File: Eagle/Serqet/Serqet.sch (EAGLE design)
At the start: 58 parts, among them U1 AD9283, U3 LTC2633CTS8-LZ8TRMPBF

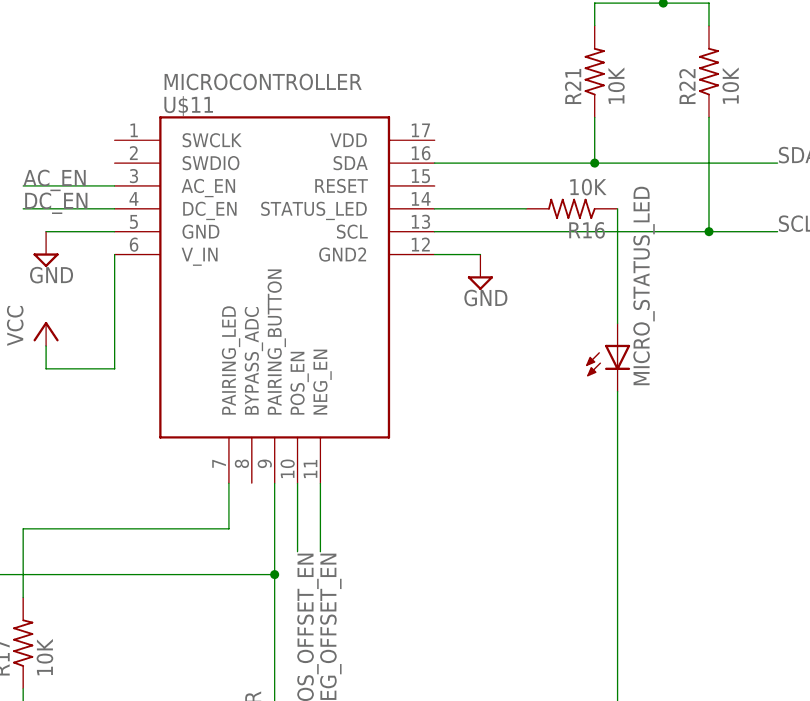
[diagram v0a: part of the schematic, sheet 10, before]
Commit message: add nets for reset and bypass adc
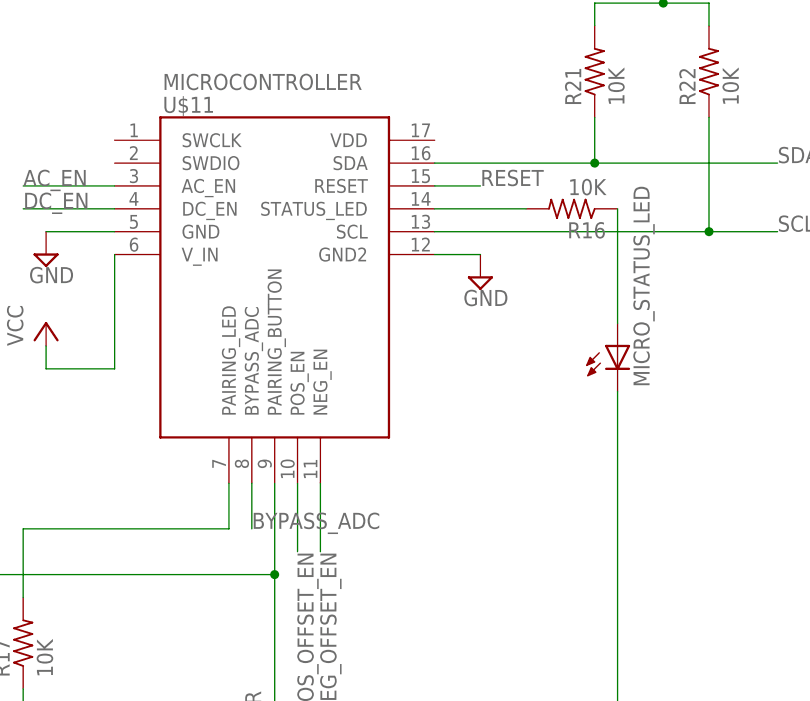
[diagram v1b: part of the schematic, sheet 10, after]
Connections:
- new net BYPASS_ADC: U$11.BYPASS_ADC
- net RESET: now also U$11.RESET
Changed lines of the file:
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@@
+</segment>
+</net>
+<net name="RESET" class="0">
+<segment>
+<pinref part="U$11" gate="G$1" pin="RESET"/>
+<wire x1="68.58" y1="66.04" x2="73.66" y2="66.04" width="0.1524" layer="91"/>
+<label x="73.66" y="66.04" size="1.778" layer="95"/>
+</segment>
+</net>
+<net name="BYPASS_ADC" class="0">
+<segment>
+<pinref part="U$11" gate="G$1" pin="BYPASS_ADC"/>
+<wire x1="48.26" y1="33.02" x2="48.26" y2="27.94" width="0.1524" layer="91"/>
+<label x="48.26" y="27.94" size="1.778" layer="95"/>
 </segment>
 </net>

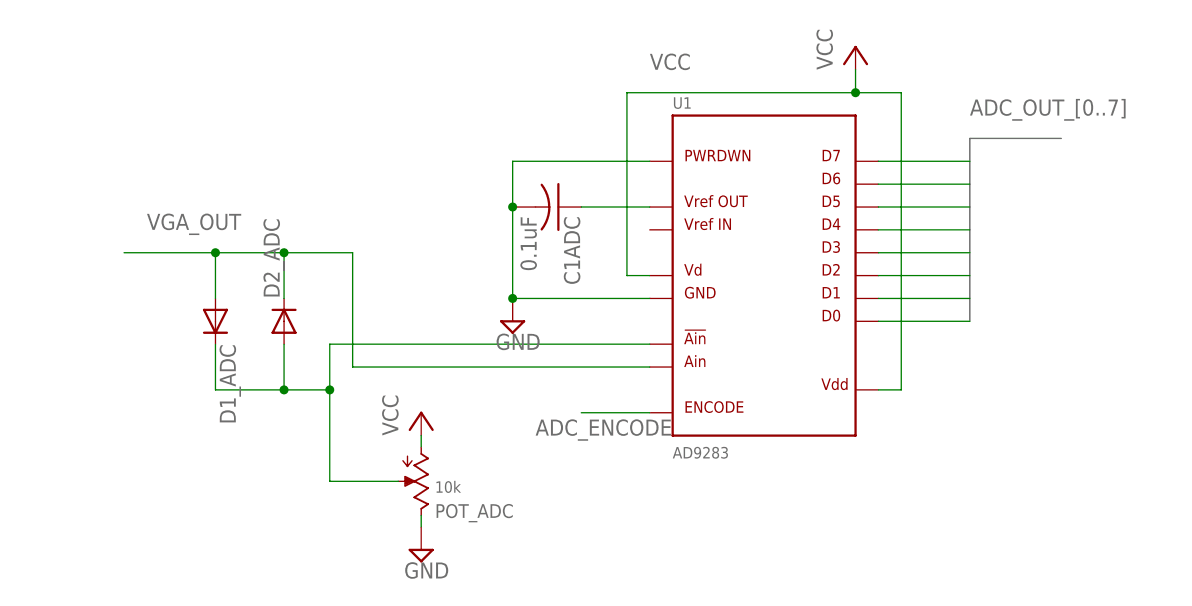
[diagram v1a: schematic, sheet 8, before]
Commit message: Added bypass resistors
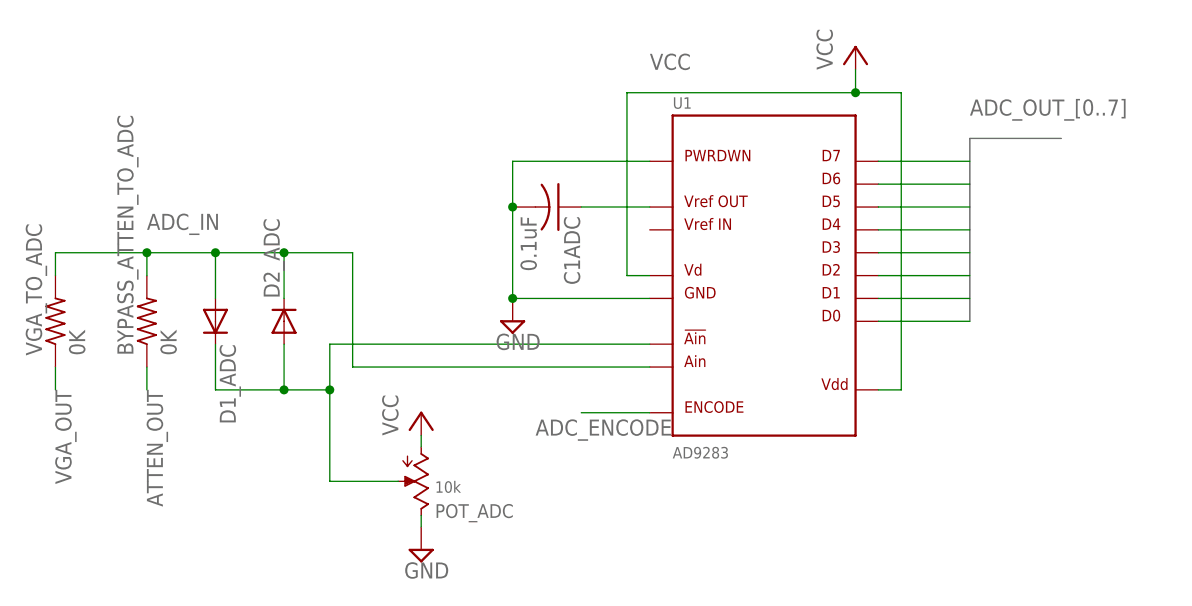
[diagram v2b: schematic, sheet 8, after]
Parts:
- added BYPASS_ATTEN_MICRO, BYPASS_ATTEN_TO_ADC, VGA_TO_ADC: 0K, resistor:R-US_R0603
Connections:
- removed net BYPASS_ADC: U$11.BYPASS_ADC
- new net ADC_IN: BYPASS_ATTEN_TO_ADC.2, D1_ADC.A, D2_ADC.C, U1.AIN, VGA_TO_ADC.2
- new net N$26: BYPASS_ATTEN_MICRO.2, U$11.BYPASS_ADC
- net ATTEN_OUT: now also BYPASS_ATTEN_MICRO.1, BYPASS_ATTEN_TO_ADC.1
- net VGA_OUT: now also VGA_TO_ADC.1; no longer D1_ADC.A, D2_ADC.C, U1.AIN
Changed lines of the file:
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@@
 <part name="C4" library="rcl" deviceset="C-US" device="C0603" value="0.1uF"/>
 <part name="BATTERY" library="con-custom" deviceset="LED_THROUGHHOLE" device=""/>
+<part name="BYPASS_ATTEN_TO_ADC" library="resistor" deviceset="R-US_" device="R0603" value="0K"/>
+<part name="VGA_TO_ADC" library="resistor" deviceset="R-US_" device="R0603" value="0K"/>
+<part name="BYPASS_ATTEN_MICRO" library="resistor" deviceset="R-US_" device="R0603" value="0K"/>
 </parts>
 <sheets>
@@
 <instance part="P+10" gate="VCC" x="68.58" y="78.74"/>
 <instance part="SUPPLY19" gate="GND" x="20.32" y="22.86"/>
+<instance part="BYPASS_ATTEN_TO_ADC" gate="G$1" x="-10.16" y="48.26" rot="R90"/>
+<instance part="VGA_TO_ADC" gate="G$1" x="-20.32" y="48.26" rot="R90"/>
 </instances>
 <busses>
@@
 </busses>
 <nets>
-<net name="VGA_OUT" class="0">
-<segment>
-<pinref part="D1_ADC" gate="1" pin="A"/>
-<wire x1="-2.54" y1="50.8" x2="-2.54" y2="55.88" width="0.1524" layer="91"/>
-<wire x1="-2.54" y1="55.88" x2="5.08" y2="55.88" width="0.1524" layer="91"/>
-<pinref part="D2_ADC" gate="1" pin="C"/>
-<wire x1="5.08" y1="55.88" x2="5.08" y2="50.8" width="0.1524" layer="91"/>
-<junction x="-2.54" y="55.88"/>
-<wire x1="5.08" y1="55.88" x2="12.7" y2="55.88" width="0.1524" layer="91"/>
-<wire x1="12.7" y1="55.88" x2="12.7" y2="43.18" width="0.1524" layer="91"/>
-<junction x="5.08" y="55.88"/>
-<pinref part="U1" gate="U" pin="AIN"/>
-<wire x1="12.7" y1="43.18" x2="45.72" y2="43.18" width="0.1524" layer="91"/>
-<wire x1="-2.54" y1="55.88" x2="-12.7" y2="55.88" width="0.1524" layer="91"/>
-<label x="-10.16" y="58.42" size="1.778" layer="95"/>
-</segment>
-</net>
 <net name="GND" class="0">
 <segment>
@@
 <pinref part="U1" gate="U" pin="D7"/>
 <wire x1="81.28" y1="66.04" x2="71.12" y2="66.04" width="0.1524" layer="91"/>
+</segment>
+</net>
+<net name="ADC_IN" class="0">
+<segment>
+<pinref part="D1_ADC" gate="1" pin="A"/>
+<wire x1="-2.54" y1="50.8" x2="-2.54" y2="55.88" width="0.1524" layer="91"/>
+<wire x1="-2.54" y1="55.88" x2="5.08" y2="55.88" width="0.1524" layer="91"/>
+<pinref part="D2_ADC" gate="1" pin="C"/>
+<wire x1="5.08" y1="55.88" x2="5.08" y2="50.8" width="0.1524" layer="91"/>
+<junction x="-2.54" y="55.88"/>
+<wire x1="5.08" y1="55.88" x2="12.7" y2="55.88" width="0.1524" layer="91"/>
+<wire x1="12.7" y1="55.88" x2="12.7" y2="43.18" width="0.1524" layer="91"/>
+<junction x="5.08" y="55.88"/>
+<pinref part="U1" gate="U" pin="AIN"/>
+<wire x1="12.7" y1="43.18" x2="45.72" y2="43.18" width="0.1524" layer="91"/>
+<wire x1="-2.54" y1="55.88" x2="-10.16" y2="55.88" width="0.1524" layer="91"/>
+<label x="-10.16" y="58.42" size="1.778" layer="95"/>
+<pinref part="BYPASS_ATTEN_TO_ADC" gate="G$1" pin="2"/>
+<wire x1="-10.16" y1="55.88" x2="-10.16" y2="53.34" width="0.1524" layer="91"/>
+<junction x="-10.16" y="55.88"/>
+<pinref part="VGA_TO_ADC" gate="G$1" pin="2"/>
+<wire x1="-10.16" y1="55.88" x2="-20.32" y2="55.88" width="0.1524" layer="91"/>
+<wire x1="-20.32" y1="55.88" x2="-20.32" y2="53.34" width="0.1524" layer="91"/>
+</segment>
+</net>
+<net name="ATTEN_OUT" class="0">
+<segment>
+<pinref part="BYPASS_ATTEN_TO_ADC" gate="G$1" pin="1"/>
+<wire x1="-10.16" y1="43.18" x2="-10.16" y2="40.64" width="0.1524" layer="91"/>
+<label x="-10.16" y="40.64" size="1.778" layer="95" rot="R270"/>
+</segment>
+</net>
+<net name="VGA_OUT" class="0">
+<segment>
+<pinref part="VGA_TO_ADC" gate="G$1" pin="1"/>
+<wire x1="-20.32" y1="43.18" x2="-20.32" y2="40.64" width="0.1524" layer="91"/>
+<label x="-20.32" y="40.64" size="1.778" layer="95" rot="R270"/>
 </segment>
 </net>
@@
 <instance part="R21" gate="G$1" x="86.36" y="78.74" rot="R90"/>
 <instance part="R22" gate="G$1" x="99.06" y="78.74" rot="R90"/>
+<instance part="BYPASS_ATTEN_MICRO" gate="G$1" x="30.48" y="35.56" rot="R270"/>
 </instances>
 <busses>
@@
 </segment>
 </net>
-<net name="BYPASS_ADC" class="0">
+<net name="N$26" class="0">
 <segment>
 <pinref part="U$11" gate="G$1" pin="BYPASS_ADC"/>
-<wire x1="48.26" y1="33.02" x2="48.26" y2="27.94" width="0.1524" layer="91"/>
-<label x="48.26" y="27.94" size="1.778" layer="95"/>
-</segment>
-</net>
+<pinref part="BYPASS_ATTEN_MICRO" gate="G$1" pin="2"/>
+<wire x1="48.26" y1="33.02" x2="48.26" y2="30.48" width="0.1524" layer="91"/>
+<wire x1="48.26" y1="30.48" x2="30.48" y2="30.48" width="0.1524" layer="91"/>
+</segment>
+</net>
+<net name="ATTEN_OUT" class="0">
+<segment>
+<pinref part="BYPASS_ATTEN_MICRO" gate="G$1" pin="1"/>
+<wire x1="30.48" y1="40.64" x2="15.24" y2="40.64" width="0.1524" layer="91"/>
+<label x="10.16" y="40.64" size="1.778" layer="95"/>
+</segment>
+</net>

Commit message: Updated names
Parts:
- renumbered C1ADC to C1_ADC, CVREG10U to C2_POWER, CVREG4.7P to C1_POWER, KNJN_FPGA1 to FPGA, LVREG2.2U to L1_POWER, OP_COUPLING to OP_AMP_COUPLING, R15 to R1_FPGA

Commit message: Updated more names
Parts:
- renumbered LED_THROUGHOLE1 to LED_THROUGHOLE, LED_THROUGHOLE2 to PAIRING_SWITCH, MCU_R_PAIR to R5_MICRO, R16 to R3_MICRO, R17 to R4_MICRO, R21 to R1_MICRO, R22 to R2_MICRO
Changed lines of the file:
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@@
 <part name="MICRO_STATUS_LED" library="led" deviceset="LED" device="CHIP-LED0805"/>
 <part name="SUPPLY25" library="supply2" deviceset="GND" device=""/>
-<part name="R16" library="resistor" deviceset="R-US_" device="R0603" value="10K"/>
-<part name="MCU_R_PAIR" library="rcl" deviceset="R-US_" device="R0603" value="10K"/>
+<part name="R3_MICRO" library="resistor" deviceset="R-US_" device="R0603" value="10K"/>
+<part name="R5_MICRO" library="rcl" deviceset="R-US_" device="R0603" value="10K"/>
 <part name="P+15" library="supply1" deviceset="VCC" device=""/>
-<part name="R17" library="resistor" deviceset="R-US_" device="R0603" value="10K"/>
-<part name="LED_THROUGHOLE1" library="con-custom" deviceset="LED_THROUGHHOLE" device=""/>
-<part name="LED_THROUGHOLE2" library="con-custom" deviceset="LED_THROUGHHOLE" device=""/>
+<part name="R4_MICRO" library="resistor" deviceset="R-US_" device="R0603" value="10K"/>
+<part name="LED_THROUGHOLE" library="con-custom" deviceset="LED_THROUGHHOLE" device=""/>
+<part name="PAIRING_SWITCH" library="con-custom" deviceset="LED_THROUGHHOLE" device=""/>
 <part name="P+16" library="supply1" deviceset="VCC" device=""/>
-<part name="R21" library="resistor" deviceset="R-US_" device="R0603" value="10K"/>
-<part name="R22" library="resistor" deviceset="R-US_" device="R0603" value="10K"/>
+<part name="R1_MICRO" library="resistor" deviceset="R-US_" device="R0603" value="10K"/>
+<part name="R2_MICRO" library="resistor" deviceset="R-US_" device="R0603" value="10K"/>
 <part name="BNC" library="SparkFun-Connectors" deviceset="BNC" device="PTH"/>
 <part name="SUPPLY1" library="supply2" deviceset="GND" device=""/>
@@
 <instance part="MICRO_STATUS_LED" gate="G$1" x="88.9" y="48.26"/>
 <instance part="SUPPLY25" gate="GND" x="88.9" y="-25.4"/>
-<instance part="R16" gate="G$1" x="83.82" y="63.5" rot="R180"/>
-<instance part="MCU_R_PAIR" gate="G$1" x="50.8" y="0" rot="R90"/>
+<instance part="R3_MICRO" gate="G$1" x="83.82" y="63.5" rot="R180"/>
+<instance part="R5_MICRO" gate="G$1" x="50.8" y="0" rot="R90"/>
 <instance part="P+15" gate="VCC" x="-15.24" y="43.18"/>
-<instance part="R17" gate="G$1" x="22.86" y="15.24" rot="R90"/>
-<instance part="LED_THROUGHOLE1" gate="G$1" x="22.86" y="-2.54" rot="R90"/>
-<instance part="LED_THROUGHOLE2" gate="G$1" x="2.54" y="22.86" rot="R180"/>
+<instance part="R4_MICRO" gate="G$1" x="22.86" y="15.24" rot="R90"/>
+<instance part="LED_THROUGHOLE" gate="G$1" x="22.86" y="-2.54" rot="R90"/>
+<instance part="PAIRING_SWITCH" gate="G$1" x="2.54" y="22.86" rot="R180"/>
 <instance part="P+16" gate="VCC" x="93.98" y="96.52"/>
-<instance part="R21" gate="G$1" x="86.36" y="78.74" rot="R90"/>
-<instance part="R22" gate="G$1" x="99.06" y="78.74" rot="R90"/>
+<instance part="R1_MICRO" gate="G$1" x="86.36" y="78.74" rot="R90"/>
+<instance part="R2_MICRO" gate="G$1" x="99.06" y="78.74" rot="R90"/>
 <instance part="BYPASS_ATTEN_MICRO" gate="G$1" x="30.48" y="35.56" rot="R270"/>
 </instances>
@@
 <label x="106.68" y="60.96" size="1.778" layer="95"/>
 <wire x1="68.58" y1="60.96" x2="99.06" y2="60.96" width="0.1524" layer="91"/>
-<pinref part="R22" gate="G$1" pin="1"/>
+<pinref part="R2_MICRO" gate="G$1" pin="1"/>
 <wire x1="99.06" y1="60.96" x2="99.06" y2="73.66" width="0.1524" layer="91"/>
 <wire x1="99.06" y1="60.96" x2="106.68" y2="60.96" width="0.1524" layer="91"/>
@@
 <label x="106.68" y="68.58" size="1.778" layer="95"/>
 <wire x1="68.58" y1="68.58" x2="86.36" y2="68.58" width="0.1524" layer="91"/>
-<pinref part="R21" gate="G$1" pin="1"/>
+<pinref part="R1_MICRO" gate="G$1" pin="1"/>
 <wire x1="86.36" y1="68.58" x2="86.36" y2="73.66" width="0.1524" layer="91"/>
 <wire x1="86.36" y1="68.58" x2="106.68" y2="68.58" width="0.1524" layer="91"/>
@@
 </segment>
 <segment>
-<pinref part="LED_THROUGHOLE1" gate="G$1" pin="NEG"/>
+<pinref part="LED_THROUGHOLE" gate="G$1" pin="NEG"/>
 <wire x1="22.86" y1="-12.7" x2="22.86" y2="-17.78" width="0.1524" layer="91"/>
 <pinref part="SUPPLY25" gate="GND" pin="GND"/>
@@
 <wire x1="88.9" y1="-17.78" x2="88.9" y2="-22.86" width="0.1524" layer="91"/>
 <junction x="88.9" y="-17.78"/>
-<pinref part="MCU_R_PAIR" gate="G$1" pin="1"/>
+<pinref part="R5_MICRO" gate="G$1" pin="1"/>
 <wire x1="50.8" y1="-5.08" x2="50.8" y2="-17.78" width="0.1524" layer="91"/>
 <wire x1="50.8" y1="-17.78" x2="88.9" y2="-17.78" width="0.1524" layer="91"/>
@@
 <pinref part="P+15" gate="VCC" pin="VCC"/>
 <wire x1="-15.24" y1="40.64" x2="-15.24" y2="22.86" width="0.1524" layer="91"/>
-<pinref part="LED_THROUGHOLE2" gate="G$1" pin="POS"/>
+<pinref part="PAIRING_SWITCH" gate="G$1" pin="POS"/>
 <wire x1="-15.24" y1="22.86" x2="-7.62" y2="22.86" width="0.1524" layer="91"/>
 </segment>
 <segment>
-<pinref part="R21" gate="G$1" pin="2"/>
+<pinref part="R1_MICRO" gate="G$1" pin="2"/>
 <wire x1="86.36" y1="83.82" x2="86.36" y2="86.36" width="0.1524" layer="91"/>
-<pinref part="R22" gate="G$1" pin="2"/>
+<pinref part="R2_MICRO" gate="G$1" pin="2"/>
 <wire x1="99.06" y1="83.82" x2="99.06" y2="86.36" width="0.1524" layer="91"/>
 <wire x1="86.36" y1="86.36" x2="93.98" y2="86.36" width="0.1524" layer="91"/>
@@
 <net name="N$22" class="0">
 <segment>
-<pinref part="MCU_R_PAIR" gate="G$1" pin="2"/>
+<pinref part="R5_MICRO" gate="G$1" pin="2"/>
 <pinref part="U$11" gate="G$1" pin="PAIRING_BUTTON"/>
 <wire x1="50.8" y1="5.08" x2="50.8" y2="22.86" width="0.1524" layer="91"/>
@@
 <wire x1="12.7" y1="22.86" x2="50.8" y2="22.86" width="0.1524" layer="91"/>
 <junction x="50.8" y="22.86"/>
-<pinref part="LED_THROUGHOLE2" gate="G$1" pin="NEG"/>
+<pinref part="PAIRING_SWITCH" gate="G$1" pin="NEG"/>
 </segment>
 </net>
 <net name="N$20" class="0">
 <segment>
-<pinref part="R16" gate="G$1" pin="2"/>
+<pinref part="R3_MICRO" gate="G$1" pin="2"/>
 <pinref part="U$11" gate="G$1" pin="STATUS_LED"/>
 <wire x1="78.74" y1="63.5" x2="68.58" y2="63.5" width="0.1524" layer="91"/>
@@
 <wire x1="45.72" y1="27.94" x2="22.86" y2="27.94" width="0.1524" layer="91"/>
 <wire x1="22.86" y1="27.94" x2="22.86" y2="20.32" width="0.1524" layer="91"/>
-<pinref part="R17" gate="G$1" pin="2"/>
+<pinref part="R4_MICRO" gate="G$1" pin="2"/>
 </segment>
 </net>
 <net name="N$24" class="0">
 <segment>
-<pinref part="LED_THROUGHOLE1" gate="G$1" pin="POS"/>
-<pinref part="R17" gate="G$1" pin="1"/>
+<pinref part="LED_THROUGHOLE" gate="G$1" pin="POS"/>
+<pinref part="R4_MICRO" gate="G$1" pin="1"/>
 <wire x1="22.86" y1="7.62" x2="22.86" y2="10.16" width="0.1524" layer="91"/>
 </segment>
@@
 <net name="N$21" class="0">
 <segment>
-<pinref part="R16" gate="G$1" pin="1"/>
+<pinref part="R3_MICRO" gate="G$1" pin="1"/>
 <pinref part="MICRO_STATUS_LED" gate="G$1" pin="A"/>
 <wire x1="88.9" y1="63.5" x2="88.9" y2="50.8" width="0.1524" layer="91"/>

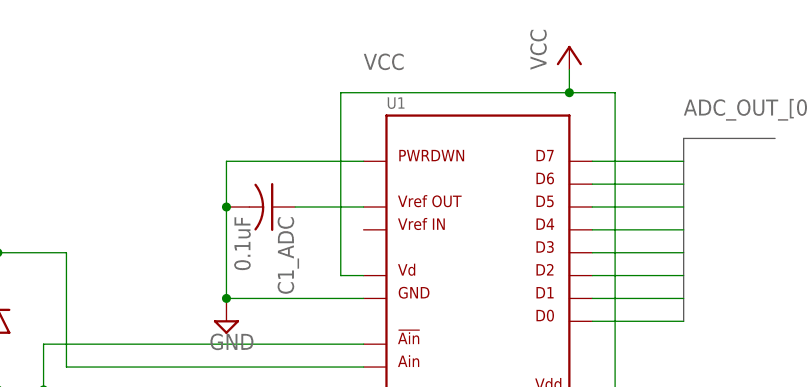
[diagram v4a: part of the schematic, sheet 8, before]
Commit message: Updated MOAR names
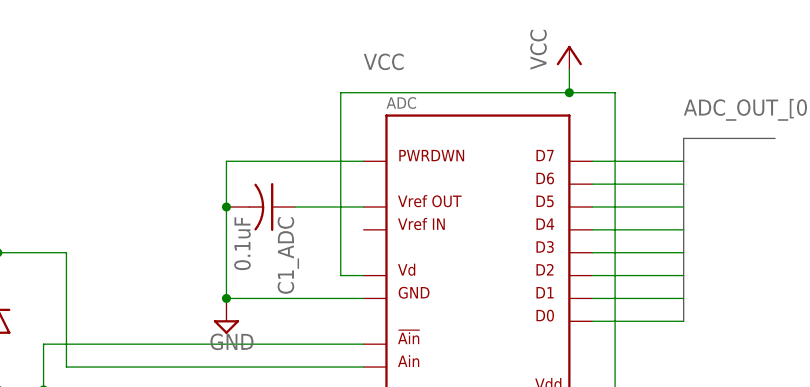
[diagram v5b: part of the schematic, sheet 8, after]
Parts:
- renumbered OP1_DCOFF to OP_AMP1_DCOFF, OP2_DCOFF to OP_AMP2_DCOFF, U$11 to MICRO, U$8 to BILATERAL_COUPLING, U$9 to BILATERAL_DCOFF, U1 to ADC, U3 to DAC

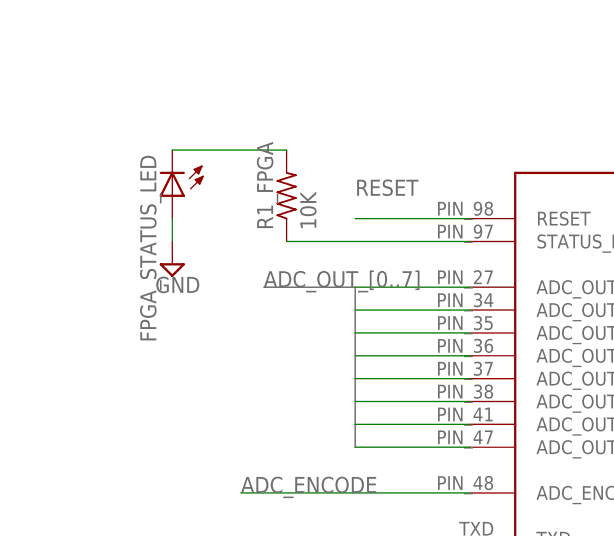
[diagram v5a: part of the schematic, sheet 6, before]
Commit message: Reversed direction of FPGA_STATUS_LED
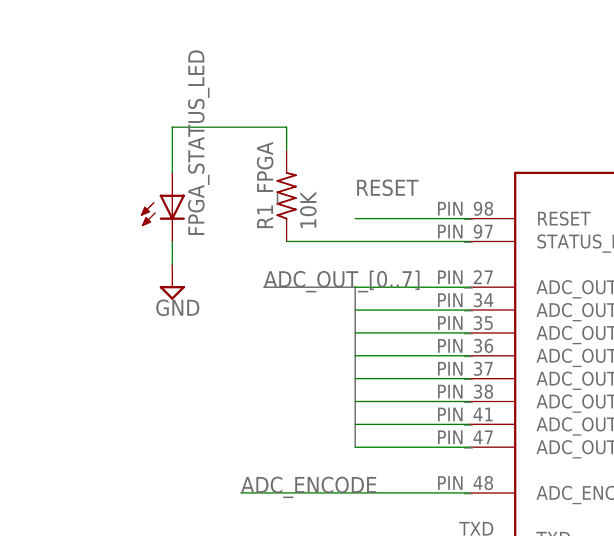
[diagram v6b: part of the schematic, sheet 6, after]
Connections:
- net GND: now also FPGA_STATUS_LED.C; no longer FPGA_STATUS_LED.A
- net N$18: now also FPGA_STATUS_LED.A; no longer FPGA_STATUS_LED.C
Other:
- moved on the sheet: FPGA_STATUS_LED
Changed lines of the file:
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@@
 <instance part="FPGA" gate="G$1" x="66.04" y="66.04"/>
 <instance part="SUPPLY20" gate="GND" x="-25.4" y="40.64"/>
-<instance part="FPGA_STATUS_LED" gate="G$1" x="-10.16" y="96.52" rot="R180"/>
+<instance part="FPGA_STATUS_LED" gate="G$1" x="-10.16" y="96.52"/>
 <instance part="R1_FPGA" gate="G$1" x="2.54" y="96.52" rot="R90"/>
-<instance part="SUPPLY21" gate="GND" x="-10.16" y="88.9"/>
+<instance part="SUPPLY21" gate="GND" x="-10.16" y="86.36"/>
 </instances>
 <busses>
@@
 </segment>
 <segment>
-<pinref part="FPGA_STATUS_LED" gate="G$1" pin="A"/>
 <pinref part="SUPPLY21" gate="GND" pin="GND"/>
-<wire x1="-10.16" y1="91.44" x2="-10.16" y2="93.98" width="0.1524" layer="91"/>
+<pinref part="FPGA_STATUS_LED" gate="G$1" pin="C"/>
+<wire x1="-10.16" y1="88.9" x2="-10.16" y2="91.44" width="0.1524" layer="91"/>
 </segment>
 </net>
@@
 </segment>
 </net>
-<net name="N$18" class="0">
-<segment>
-<pinref part="R1_FPGA" gate="G$1" pin="2"/>
-<pinref part="FPGA_STATUS_LED" gate="G$1" pin="C"/>
-<wire x1="-10.16" y1="101.6" x2="2.54" y2="101.6" width="0.1524" layer="91"/>
-</segment>
-</net>
 <net name="RESET" class="0">
 <segment>
@@
 </segment>
 </net>
+<net name="N$18" class="0">
+<segment>
+<pinref part="FPGA_STATUS_LED" gate="G$1" pin="A"/>
+<wire x1="-10.16" y1="99.06" x2="-10.16" y2="104.14" width="0.1524" layer="91"/>
+<wire x1="-10.16" y1="104.14" x2="2.54" y2="104.14" width="0.1524" layer="91"/>
+<pinref part="R1_FPGA" gate="G$1" pin="2"/>
+<wire x1="2.54" y1="104.14" x2="2.54" y2="101.6" width="0.1524" layer="91"/>
+</segment>
+</net>
